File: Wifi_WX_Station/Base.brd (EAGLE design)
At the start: 100 x 81.3 mm, 62 parts, among them IC1 25LC512, IC2 3.3v, IC3 PIC24FJ128GA008, Q2 32Khz, X1 MINI-USB-VERT

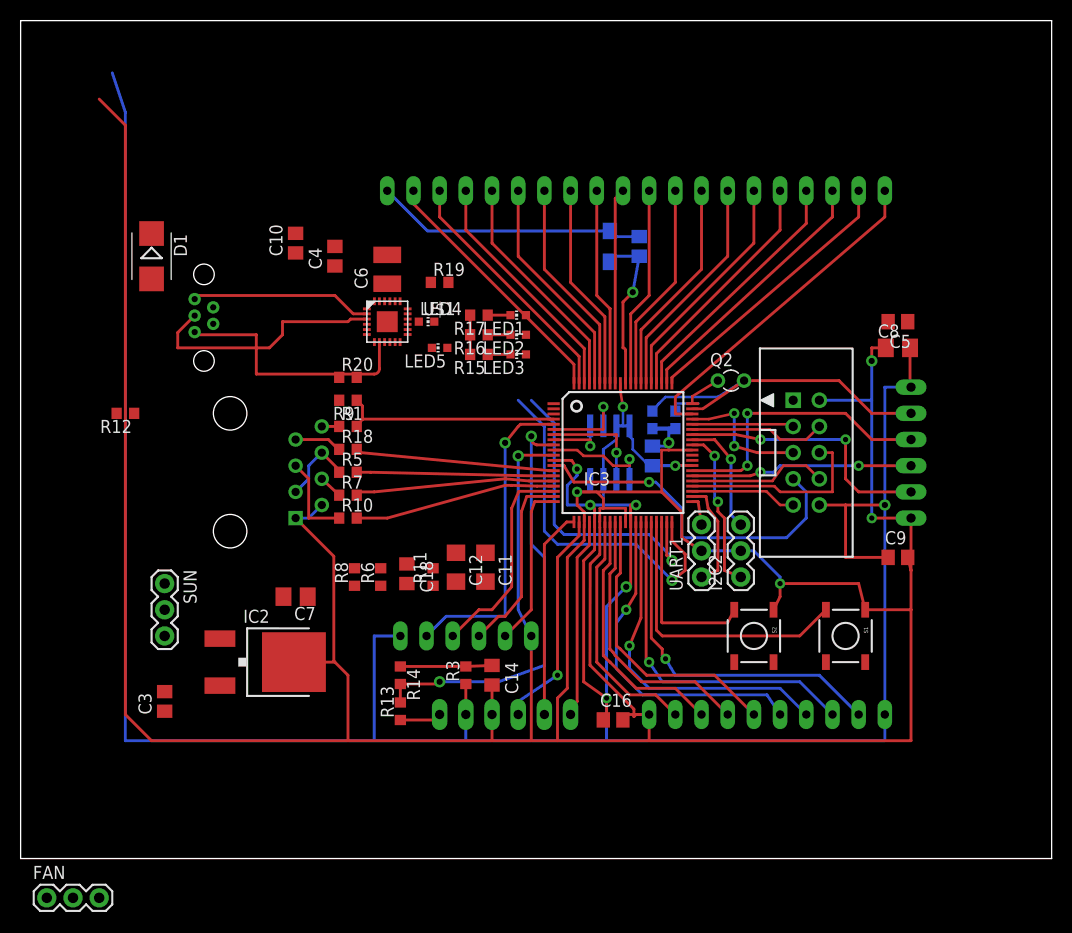
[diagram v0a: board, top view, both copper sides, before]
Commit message: added all the small boards, renamed Wifi module as RH and LH version
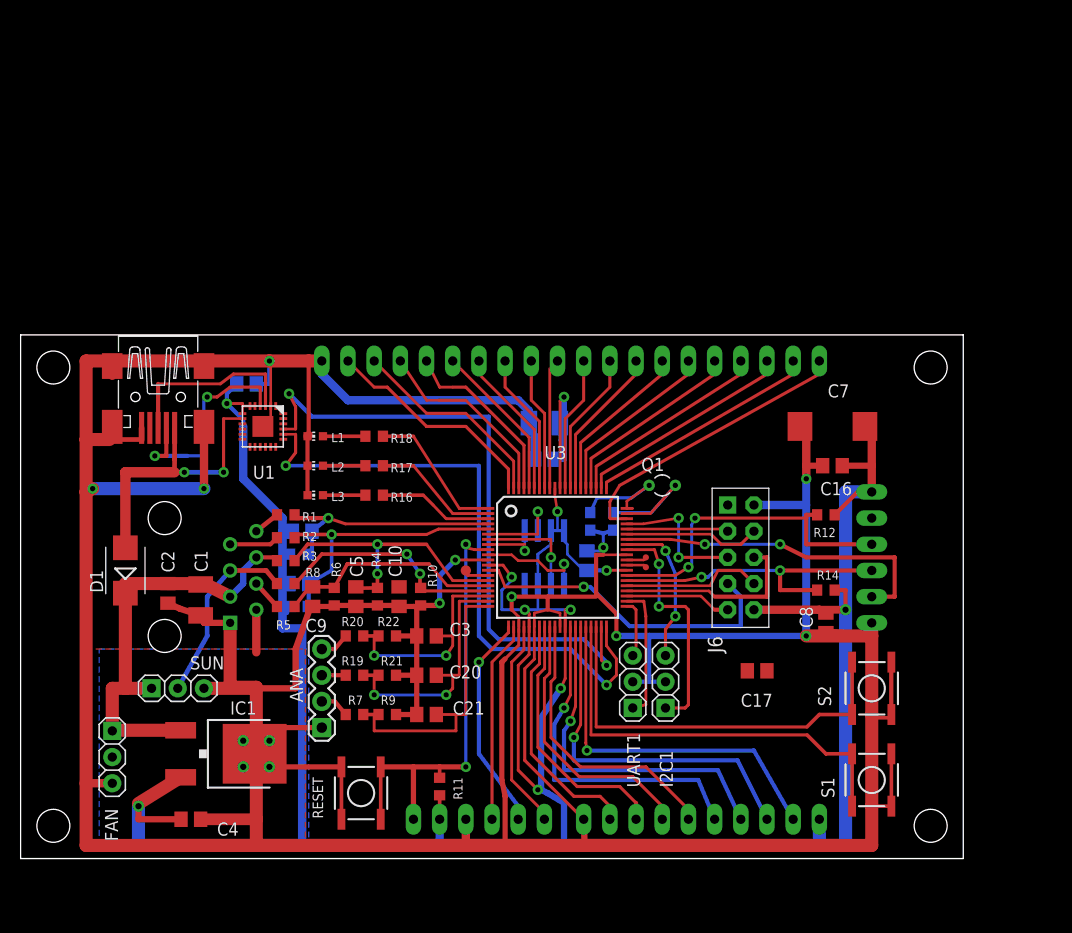
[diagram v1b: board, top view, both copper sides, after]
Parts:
- removed ANA_IN: (no value), con-lsta:FE06
- removed BHT: MA1X06, wifi_WX:1X06
- removed I2C2: (no value), SparkFun-Connectors:1X03
- removed IC2: 3.3v, Stofer:DPACK
- removed IC3: PIC24FJ128GA008, wifi_WX:TQFP80-12X12
- removed JP1: (no value), wifi_WX:1X06_PIKIT
- removed JP2: M05X2SHD, wifi_WX:2X5-SHROUDED
- removed LED1, LED2, LED3, LED4, LED5: (no value), led:CHIP-LED0603
- removed Q2: 32Khz, crystal:TC26V
- removed U$1: CP2104-GM, wifi_WX:QFN24_4X4
- removed U$3: RJ45-8VERT, wifi_WX:RJ45_VERT
- removed X1: MINI-USB-VERT, wifi_WX:USB_MINI_VERT
- added ANA: (no value), SparkFun-Connectors:1X04
- added C19, C20, C21: 0.1uF, rcl:C0805
- added I2C1: (no value), wifi_WX:1X03
- added J1: RJ45-8VERT, wifi_WX:RJ45_VERT
- added J5: MA1X06, wifi_WX:1X06
- added J6: M05X22X5FE, wifi_WX:2X5FEMALE
- added JPROG: (no value), wifi_WX:1X06_PIKIT
- added L1: grn, led:CHIP-LED0603
- added L2: ambr, led:CHIP-LED0603
- added L3: red, led:CHIP-LED0603
- added Q1: 32Khz, crystal:TC26V
- added R2: 120o, rcl:R0603
- added R21, R22: 26.1K, rcl:R0603
- added R4: 10k, rcl:R0603
- added RESET: SWITCH-MOMENTARY-2SMD, SparkFun-Electromechanical:TACTILE_SWITCH_SMD
- added TP1, TP2: TPTP06R, 1AA_Stofer:TP06R
- added TP3: TPTP10R, 1AA_Stofer:TP10R
- added U1: CP2104-GM, wifi_WX:QFN24_4X4
- added U2: 25LC512, microchip:SO-08
- added U3: PIC24FJ128GA008, wifi_WX:TQFP80-12X12
- added USB: MINI-USB-32005-301, wifi_WX:32005-301
- C1: value 22p -> 22u/10v; device rcl:C0603 -> rcl:SMC_B
- C10, C9: value 0.1u -> 2.2uF
- C11: value 2.2u -> 0.1uF; device rcl:C1206 -> rcl:C0805
- C12: value 2.2u -> 22uF/10V; device rcl:C1206 -> rcl:SMC_B
- C13: value 0.1uf -> 0.1uF
- C14: value 1u -> 22p; device rcl:C0805 -> rcl:C0603
- C15: value 10uf/6v -> 22p; device rcl:SMC_A -> rcl:C0603
- C16, C17, C18, C3, C4, C5: value 0.1u -> 0.1uF
- C2: value 22p -> 0.1uF; device rcl:C0603 -> rcl:C0805
- C6: value 4.7u -> 0.1uF; device rcl:C1210 -> rcl:C0805
- C7: value 22u/10v -> 330uF/6V; device rcl:R/2012-12R -> rcl:SMC_D
- C8: value 100u/4v -> 0.1uF; device rcl:R/2012-12R -> rcl:C0805
- FAN, SUN, UART1: device SparkFun-Connectors:1X03 -> wifi_WX:1X03
- IC1: value 25LC512 -> 3.3v; device microchip:SO-08 -> Stofer:DPACK
- R1: value 120 -> 120o
- R10: value 14k -> 26.1K
- R11: value 26.4K -> 10k
- R12: value 4.7k -> 4.7K
- R13: value 120 -> 4.7k
- R14: value 10k -> 4.7K
- R15: value 1k -> 4.7k
- R18: value 120 -> 470o
- R19, R20: value 1k -> 14k
- R5: value 10k -> 8.2k
- R6: value 10k -> 26.1k
- R7: value 6.8k -> 14k
- R8: value 26.4K -> 14k
- R9: value 4.7k -> 26.1K
- SV1, SV2, SV3: device con-lsta:FE10 -> wifi_WX:FE10
- moved R12 68.7 mm to (78.1, 33.3)
- moved C5 59.0 mm to (32.5, 25.4), turned to 270 degrees
- moved C9 56.9 mm to (28.3, 25.4), turned to 270 degrees
- moved C4 56.4 mm to (16.5, 3.81), turned to 0 degrees
- moved C7 54.6 mm to (78.7, 41.9)
- moved C2 52.0 mm to (14.3, 25.7), flipped to the top
- moved C1 47.2 mm to (17.5, 25.1), flipped to the top
- moved IC1 47.0 mm to (20.3, 10.2), flipped to the top, turned to 270 degrees
- moved R14 42.1 mm to (78.1, 26.0), turned to 180 degrees
- moved R19 39.0 mm to (32.4, 17.8)
- moved C10 35.7 mm to (36.7, 25.4), turned to 270 degrees
- moved C16 32.6 mm to (78.7, 38.1), turned to 180 degrees
- moved R9 30.7 mm to (35.6, 14.0)
- moved D1 30.6 mm to (10.2, 27.9), turned to 90 degrees
- moved R15 30.0 mm to (27.0, 24.4), flipped to the bottom, turned to 0 degrees
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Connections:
- removed net N$43: ANA_IN.5, IC3.20
- removed net N$46: LED4.A, R19.1
- removed net N$64: ANA_IN.4, IC3.19
- removed net N$65: ANA_IN.3, IC3.18
- removed net N$67: LED5.A, R20.1
- removed net N$68: LED4.C, U$1.14
- removed net N$69: LED5.C, U$1.13
- new net N$14: TP2.TP, U3.49
- new net N$18: L3.A, R16.2
- new net N$20: L2.A, R17.2
- new net N$21: L1.A, R18.2
- new net N$4: TP1.TP, U3.50
- new net N$5: R18.1, U3.1
- net +3V3: now also C11.2, C18.1, C19.2, C6.1, C7.+, C8.1, J5.6, J6.10, JPROG.2, R11.1, R12.1, R13.2, R14.1, R15.2, U1.5, U1.6, U1.7, U2.3, U2.7, U2.8, U3.12, U3.25, U3.32, U3.48, U3.71; no longer ANA_IN.1, BHT.6, C3.1, C5.1, C8.+, C9.1, IC1.7, IC1.8, IC2.3, IC3.12, IC3.25, IC3.32, IC3.48, IC3.71, JP1.2, JP2.10, R12.2, R19.2, R20.2, R3.1, R9.2, U$1.5, U$1.6, U$1.7
- net +5V: now also C1.+, C2.1, FAN.1, IC1.1, J1.P$3, J1.P$6, R3.1; no longer C10.1, C7.+, IC2.1, R5.1, U$3.P$3, U$3.P$6
- net BARO_CS: now also J5.2, U3.54; no longer BHT.2, IC3.54
- net GND: now also ANA.1, C1.-, C12.-, C15.2, C20.2, C21.2, C8.2, FAN.3, I2C1.2, J1.P$1, J1.P$2, J5.1, J6.2, JPROG.3, L1.C, L2.C, L3.C, R10.1, R21.1, R22.1, R4.1, R9.1, RESET.3, RESET.4, S1.2, S2.2, U1.2, U1.25, U2.4, U3.11, U3.23, U3.26, U3.31, U3.51, USB.5_USB_GND, USB.M1, USB.M2, USB.M3, USB.M4; no longer ANA_IN.6, BHT.1, C1.2, C11.2, C12.2, C15.-, C8.-, I2C2.2, IC2.4, IC3.11, IC3.23, IC3.26, IC3.31, IC3.51, JP1.3, JP2.2, R11.1, R15.2, R16.2, R17.2, R8.1, U$1.2, U$1.25, U$3.P$1, U$3.P$2, X1.P$5
- net MCU_RESET_: now also JPROG.1, R11.2, RESET.1, RESET.2, U3.9; no longer IC3.9, R13.2, R14.2
- net MRF_CS_: now also J6.5, U3.57; no longer IC3.57, JP2.5
- net MRF_HIBER: now also J6.3, U3.56; no longer IC3.56, JP2.3
- net MRF_RESET_: now also J6.4, U3.55; no longer IC3.55, JP2.4
- net MRF_SCK: now also J6.8, U3.45; no longer IC3.45, JP2.8
- net MRF_SDI: now also J6.9, U3.43; no longer IC3.43, JP2.9
- net MRF_SDO: now also J6.6, U3.44; no longer IC3.44, JP2.6
- net N$1: now also I2C1.1, U3.52; no longer I2C2.1, IC3.52
- net N$10: now also U3.61; no longer IC3.61
- net N$11: now also U3.62; no longer IC3.62
- net N$12: now also U3.63; no longer IC3.63
- net N$13: now also U3.64; no longer IC3.64
- net N$15: now also U3.65; no longer IC3.65
- net N$16: now also JPROG.5, U3.21; no longer IC3.21, JP1.5
- net N$17: now also JPROG.4, U3.22; no longer IC3.22, JP1.4
- net N$19: now also C12.+, U3.70; no longer C15.+, IC3.70
- net N$2: now also C15.1, Q1.2, U3.59; no longer BHT.5, C1.1, IC3.59, Q2.2
- net N$22: now also C21.1, R7.2, R9.2, U3.20; no longer C14.1, R14.1, R3.2
- net N$23: now also ANA.4, R20.1; no longer LED1.C, R17.1
- net N$24: now also C20.1, R19.2, R21.2, U3.19; no longer JP1.1, R13.1
- net N$25: now also U2.2, U3.7; no longer IC1.2, IC3.7
- net N$26: now also U3.66; no longer IC3.66
- net N$27: now also U2.1, U3.10; no longer IC1.1, IC3.10
- net N$28: now also C3.1, R20.2, R22.2, U3.18; no longer LED2.C, R16.1
- net N$29: now also U2.6, U3.6; no longer IC1.6, IC3.6
- net N$3: now also C10.1; no longer C6.1, U$1.16
- net N$30: now also ANA.3, R19.1; no longer LED3.C, R15.1
- net N$31: now also ANA.2, R7.1; no longer IC3.1, LED1.A
- net N$32: now also U2.5, U3.8; no longer IC1.5, IC3.8
- net N$33: now also R17.1, U3.2; no longer IC3.2, LED2.A
- net N$34: now also R16.1, U3.3; no longer IC3.3, LED3.A
- net N$35: now also U3.67; no longer IC3.67
- net N$36: now also U3.68; no longer IC3.68
- net N$37: now also S2.4, U3.38; no longer IC3.38
- net N$38: now also S1.4, U3.37; no longer IC3.37
- net N$40: now also U3.69; no longer IC3.69
- net N$41: now also U3.72; no longer IC3.72
- net N$42: now also U3.58; no longer IC3.58
- net N$44: now also U3.41; no longer IC3.41
- net N$45: now also U3.42; no longer IC3.42
- net N$47: now also U3.27; no longer IC3.27
- net N$48: now also U3.28; no longer IC3.28
- net N$49: now also U3.29; no longer IC3.29
- net N$50: now also U3.30; no longer IC3.30
- net N$51: now also U3.33; no longer IC3.33
- net N$52: now also U3.34; no longer IC3.34
- net N$53: now also U3.35; no longer IC3.35
- net N$54: now also U3.36; no longer IC3.36
- net N$55: now also U3.73; no longer IC3.73
- net N$56: now also U3.74; no longer IC3.74
- net N$57: now also U3.75; no longer IC3.75
- net N$58: now also U3.76; no longer IC3.76
- net N$59: now also U3.77; no longer IC3.77
- net N$6: now also I2C1.3, U3.53; no longer I2C2.3, IC3.53
- net N$60: now also U3.78; no longer IC3.78
- net N$61: now also U3.79; no longer IC3.79
- net N$62: now also U3.80; no longer IC3.80
- net N$63: now also JPROG.6, U3.24; no longer IC3.24, JP1.6
- net N$66: now also C5.1, R3.2, R4.2, U3.15; no longer C18.1, IC3.15, R5.2, R6.2
- net N$7: now also C14.1, Q1.1, U3.60; no longer C2.1, IC3.60, Q2.1
- net N$8: now also TP3.TP, U3.14; no longer ANA_IN.2, IC3.5
- net N$9: now also U1.8, USB.1_VBUS; no longer U$1.8, X1.P$1
- net RAIN_CNT_IN: now also J1.P$7, R2.1; no longer R18.1, U$3.P$7
- net RAIN_COUNT: now also C11.1, R15.1, R2.2, U3.5; no longer IC3.14, R12.1, R18.2
- net SCL1: now also J5.4, R12.2, U3.47; no longer BHT.4, IC3.47
- net SDA1: now also J5.3, R14.2, U3.46; no longer BHT.3, IC3.46
- net SUN_ADC_IN: now also R8.2, U3.17; no longer C12.1, IC3.17, R11.2
- net SUN_IN: now also J1.P$5, R8.1; no longer R10.1, U$3.P$5
- net USB_D+: now also U1.3, USB.3_D+; no longer U$1.3, X1.P$3
- net USB_D-: now also U1.4, USB.2_D-; no longer U$1.4, X1.P$2
- net USB_RXD: now also U1.20, U3.40; no longer IC3.40, U$1.20
- net USB_TXD: now also U1.21, U3.39; no longer IC3.39, U$1.21
- net WIFI_INT_: now also J6.7, U3.13; no longer IC3.13, JP2.7
- net WIND_ADC_IN: now also C9.1, R5.2, R6.2, U3.16; no longer C11.1, IC3.16, R7.2, R8.2
- net WIND_COUNT: now also C19.1, R13.1, U3.4; no longer IC3.4, R9.1
- net WIND_COUNT_IN: now also J1.P$8; no longer U$3.P$8
- net WIN_DIR_IN: now also J1.P$4, R5.1; no longer R7.1, U$3.P$4
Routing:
- net GND: track 424.0 -> 553.0 mm, vias 6 -> 14
- net +5V: track 7.47 -> 42.3 mm
- net USB_TXD: track 30.0 -> 62.7 mm, vias 1 -> 2
- net N$8: track 30.8 -> 2.51 mm, vias 1 -> 0
- net USB_RXD: track 34.9 -> 60.5 mm, vias 1 -> 2
- net N$37: track 17.6 -> 40.1 mm
- net USB_D-: track 0.00 -> 21.9 mm, vias 0 -> 2
- net N$24: track 4.03 -> 25.2 mm, vias 0 -> 2
- net N$65: track 20.6 -> 0.00 mm
- net N$2: track 33.3 -> 13.2 mm
- net N$22: track 8.89 -> 28.5 mm
- net N$28: track 2.21 -> 21.4 mm, vias 0 -> 2
- net N$64: track 18.2 -> 0.00 mm
- net N$43: track 16.0 -> 0.00 mm
- net N$5: track 0.00 -> 14.0 mm
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- added copper zone on layer 1, net GND
- added copper zone on layer 16, net GND
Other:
- board size 100 x 81.3 mm -> 91.4 x 50.8 mm
- board text added: "1"
- board text added: "RV-BUILDERS PRODUCTS 2013"
- board text added: "Wunder Weather Station"

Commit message: updated BOM with all prices- As Checked in to BATCH PCB
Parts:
- removed C17: 0.1uF, rcl:C0805
- added R23, R24: 4.7K, rcl:R0603
- ANA: device SparkFun-Connectors:1X04 -> wifi_WX:1X04
- FAN, SUN: device wifi_WX:1X03 -> wifi_WX:1X3_MOLEX_KK
- IC1: device Stofer:DPACK -> wifi_WX:DPACK
- J5: value MA1X06 -> (none); device wifi_WX:1X06 -> wifi_WX:1X5_MOLEX_KK
- Q1: value 32Khz -> 32.768Khz; device crystal:TC26V -> wifi_WX:CRYSTAL32_SMT
- RESET, S1, S2: device SparkFun-Electromechanical:TACTILE_SWITCH_SMD -> wifi_WX:TACTILE_SWITCH_SMD
- SV1, SV2, SV3: value (none) -> M10"; device wifi_WX:FE10 -> wifi_WX:1X10
- TP1, TP2: value TPTP06R -> TP; device 1AA_Stofer:TP06R -> wifi_WX:TP06R
- TP3: value TPTP10R -> TP; device 1AA_Stofer:TP10R -> wifi_WX:TP06R
- moved TP1 17.5 mm to (43.2, 27.9)
- moved TP3 17.1 mm to (60.3, 28.3)
- moved SV1 11.4 mm to (54.6, 3.81)
- moved SV3 11.4 mm to (52.1, 48.3)
- moved SV2 11.4 mm to (77.5, 48.3)
- moved I2C1 10.8 mm to (72.4, 12.7), turned to 0 degrees
- moved J5 7.10 mm to (79.4, 22.9)
- moved Q1 5.85 mm to (63.5, 41.9), flipped to the bottom
- moved UART1 5.28 mm to (62.2, 12.7), turned to 180 degrees
- moved FAN 4.96 mm to (12.1, 13.7), flipped to the bottom
- moved SUN 4.07 mm to (12.7, 13.3)
- moved R12 2.22 mm to (75.9, 33.3), turned to 270 degrees
- moved R14 2.22 mm to (75.9, 26.0), turned to 90 degrees
- moved RESET 1.91 mm to (31.1, 6.35)
- moved IC1 1.42 mm to (19.1, 9.53)
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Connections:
- removed net N$1: I2C1.1, U3.52
- removed net N$3: C10.1
- removed net N$6: I2C1.3, U3.53
- new net SCL2: I2C1.1, R24.2, U3.52
- new net SDA2: I2C1.3, R23.2, U3.53
- net +3V3: now also J5.5, R23.1, R24.1; no longer C17.1, J5.6
- net GND: no longer C17.2
- net N$14: now also TP3.TP_1; no longer TP2.TP
- net N$2: now also Q1.P$3; no longer Q1.2
- net N$4: now also TP2.TP_1; no longer TP1.TP
- net N$7: now also Q1.P$2; no longer Q1.1
- net N$8: now also TP1.TP_1; no longer TP3.TP
- net SUN_ADC_IN: now also C10.1
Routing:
- net GND: track 553.0 -> 590.7 mm
- net SCL2: track 0.00 -> 30.5 mm, vias 0 -> 3
- net SDA2: track 0.00 -> 29.7 mm, vias 0 -> 2
- net N$1: track 22.8 -> 0.00 mm, vias 2 -> 0
- net N$6: track 14.8 -> 0.00 mm, vias 2 -> 0
- net N$44: track 5.79 -> 14.6 mm
- net N$7: track 10.9 -> 16.8 mm, vias 0 -> 1
- net SDA1: track 29.6 -> 25.0 mm
- net N$45: track 13.0 -> 16.8 mm
- net N$37: track 40.1 -> 43.6 mm
- net SCL1: track 32.4 -> 29.0 mm
- net +3V3: track 299.0 -> 296.5 mm
- net +5V: track 42.3 -> 44.5 mm, vias 0 -> 1
- net SUN_ADC_IN: track 22.7 -> 24.7 mm
- net MCU_RESET_: track 43.6 -> 45.5 mm
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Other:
- board text added: "Baro & Hygro"
- board text added: "J6"
- board text added: "This is NOT an Ethernet port"
- board text added: "WiFi"

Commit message: Wind speed board and base station rework to rev HW 1.2
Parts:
- added +5V: (no value), wifi_WX:1X3_MOLEX_KK
- added D2: MBR0520LT, diode:SOD123
- added RAIN: M02, wifi_WX:1X02
- ANA: device wifi_WX:1X04 -> wifi_WX:1X05
- R13: value 4.7k -> 2.2K
- TP1: value TP -> TP10R; device wifi_WX:TP06R -> wifi_WX:TP10R
- TP2, TP3: value TP -> TP6R
- moved UART1 15.7 mm to (77.5, 8.89), turned to 90 degrees
- moved I2C1 6.35 mm to (77.5, 16.5), turned to 90 degrees
- moved FAN 4.14 mm to (12.4, 17.8)
- moved C3 2.62 mm to (40.0, 19.1)
- moved R22 2.62 mm to (36.2, 19.1)
- moved R20 2.54 mm to (32.4, 19.1)
- moved C20 1.42 mm to (40.0, 16.5)
- moved R21 1.42 mm to (36.2, 16.5)
- moved JPROG 1.27 mm to (43.2, 3.81)
- moved R11 1.27 mm to (39.4, 6.99)
- moved S1 1.27 mm to (82.5, 6.35)
- moved ANA 1.27 mm to (29.2, 11.4)
- moved R19 1.27 mm to (32.4, 16.5)
- moved C21 0.64 mm to (40.0, 14.0)
- moved R9 0.63 mm to (36.2, 14.0)
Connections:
- new net N$1: D2.C, R2.2
- net +5V: now also +5V.1, ANA.5
- net GND: now also +5V.3, RAIN.1
- net RAIN_CNT_IN: now also RAIN.2
- net RAIN_COUNT: now also D2.A; no longer R2.2
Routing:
- net GND: track 590.7 -> 612.1 mm, vias 14 -> 15
- net N$45: track 16.8 -> 34.4 mm, vias 0 -> 1
- net N$44: track 14.6 -> 31.8 mm
- net +5V: track 44.5 -> 55.6 mm, vias 1 -> 0
- net USB_D-: track 21.9 -> 13.7 mm, vias 2 -> 0
- net RAIN_CNT_IN: track 4.81 -> 12.6 mm
- net N$1: track 0.00 -> 6.35 mm
- net N$9: track 28.2 -> 23.5 mm, vias 2 -> 0
- net SCL2: track 30.5 -> 34.9 mm, vias 3 -> 4
- net RAIN_COUNT: track 27.5 -> 23.9 mm
- net N$28: track 21.4 -> 24.3 mm
- net +3V3: track 296.5 -> 294.6 mm
- net USB_RXD: track 60.5 -> 59.3 mm
- net WIND_COUNT: track 24.2 -> 25.1 mm
- net SUN_ADC_IN: track 24.7 -> 25.6 mm
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
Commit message: Revision B.1
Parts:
- C5: value 0.1uF -> 2.2uF
- moved Q1 1.27 mm to (63.5, 40.6)
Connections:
- removed net N$37: S2.3, S2.4, U3.38
- removed net N$38: S1.3, S1.4, U3.37
- new net SW_S1: S1.3, S1.4, U1.13, U3.37
- new net SW_S2: S2.3, S2.4, U1.12, U3.38
- net MCU_RESET_: now also U1.14
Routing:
- net SW_S2: track 0.00 -> 100.4 mm, vias 0 -> 4
- net SW_S1: track 0.00 -> 96.1 mm, vias 0 -> 4
- net N$37: track 43.3 -> 0.00 mm
- net N$38: track 42.6 -> 0.00 mm
- net MCU_RESET_: track 45.5 -> 75.1 mm, vias 2 -> 3
- net GND: track 612.1 -> 619.7 mm
- net WIFI_INT_: track 31.8 -> 33.8 mm
- net N$2: track 13.0 -> 11.8 mm
- net N$7: track 16.8 -> 15.5 mm
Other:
- board text added: "NOT Ethernet !"
- board text added: "PCB Revision B.2"
- board text added: "PIC24FJ256GA108"
- board text removed: "This is NOT an Ethernet port"

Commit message: 
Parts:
- C9: value 2.2uF -> 0.1uF
- R6: value 26.1k -> 26.1K
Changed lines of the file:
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@@
 <attribute name="NAME" x="24.765" y="22.225" size="0.889" layer="25"/>
 </element>
-<element name="R6" library="rcl" package="R0603" value="26.1k" x="30.4165" y="25.4" smashed="yes" rot="R90">
+<element name="R6" library="rcl" package="R0603" value="26.1K" x="30.4165" y="25.4" smashed="yes" rot="R90">
 <attribute name="NAME" x="31.0515" y="27.305" size="0.889" layer="25" rot="R90"/>
 </element>
-<element name="C9" library="rcl" package="C0805" value="2.2uF" x="28.321" y="25.4" smashed="yes" rot="R270">
+<element name="C9" library="rcl" package="C0805" value="0.1uF" x="28.321" y="25.4" smashed="yes" rot="R270">
 <attribute name="NAME" x="27.559" y="21.2725" size="1.016" layer="25" rot="R90"/>
 </element>

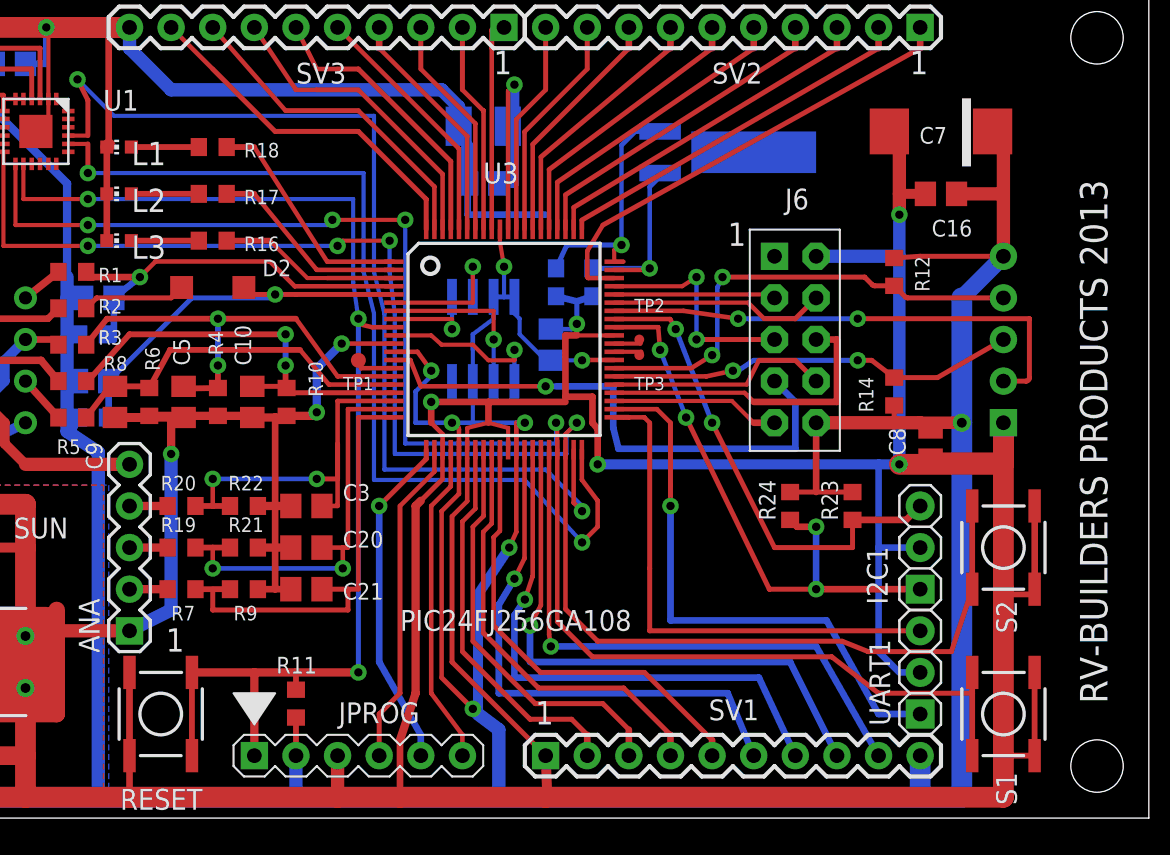
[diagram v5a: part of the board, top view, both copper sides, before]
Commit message: Changed to RJ11 connector for Baro_temp_hyg  on base board -- Cleaned up some silk screen stuff Added new RJ11 based Baro_Temp_Hyg board layout
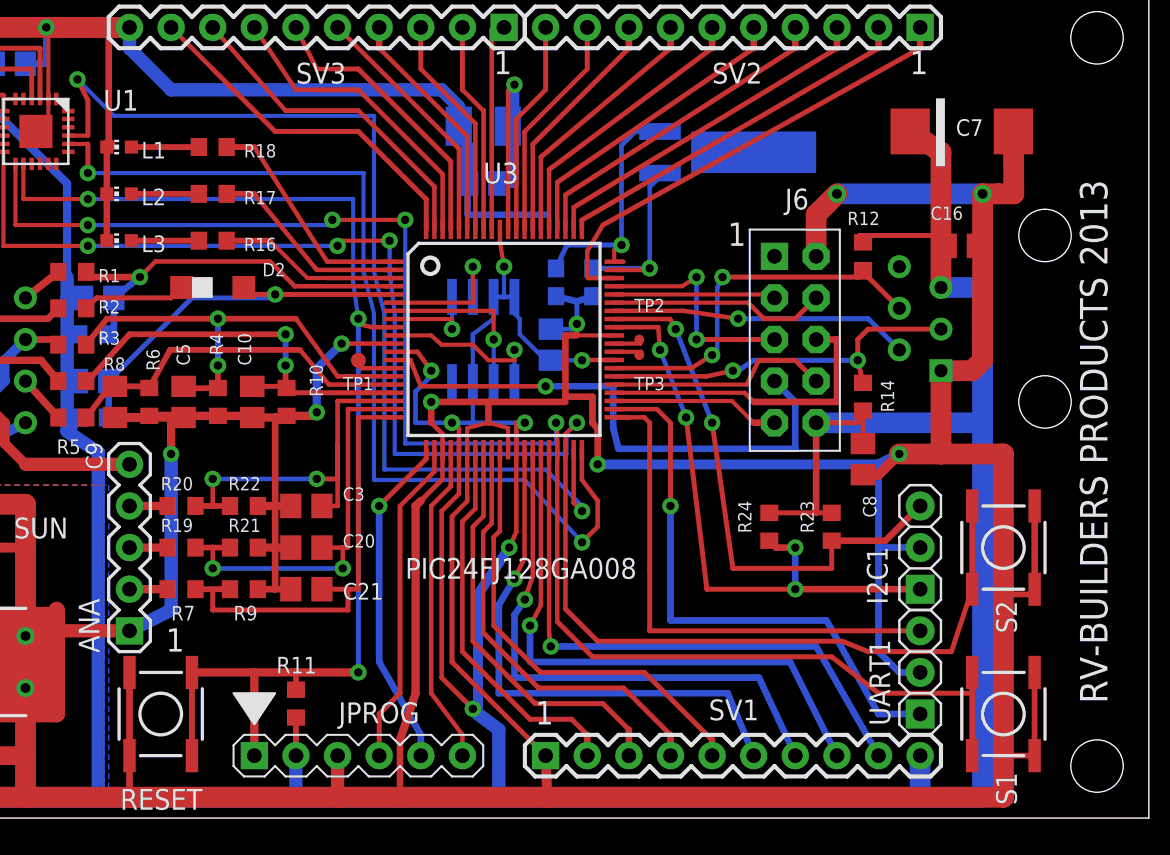
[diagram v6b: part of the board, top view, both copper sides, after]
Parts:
- J5: value (none) -> RJ11-6RJ11-VERT_LP; device wifi_WX:1X5_MOLEX_KK -> wifi_WX:RJ11-6-VERT
- moved J5 8.26 mm to (82.5, 30.5), turned to 270 degrees
- moved C8 4.24 mm to (74.0, 21.9)
- moved C16 3.42 mm to (80.0, 34.9), turned to 0 degrees
- moved R12 2.13 mm to (74.0, 34.3)
- moved R14 1.93 mm to (74.0, 25.7)
- moved R23 1.80 mm to (72.1, 17.8)
- moved R24 1.80 mm to (68.3, 17.8)
- moved C7 1.27 mm to (80.0, 41.9), turned to 0 degrees
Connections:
- net +3V3: now also J5.P$5; no longer J5.5
- net BARO_CS: now also J5.P$2; no longer J5.2
- net GND: now also J5.P$1; no longer J5.1
- net SCL1: now also J5.P$4; no longer J5.4
- net SDA1: now also J5.P$3; no longer J5.3
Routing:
- net BARO_CS: track 30.7 -> 18.2 mm, vias 2 -> 1
- net +3V3: track 294.6 -> 301.0 mm, vias 10 -> 9
- net SCL1: track 29.0 -> 23.5 mm
- net SDA2: track 29.7 -> 33.2 mm
- net GND: track 619.7 -> 621.8 mm, vias 15 -> 16
- net SDA1: track 25.0 -> 23.1 mm
- net SCL2: track 34.9 -> 36.4 mm
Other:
- board text added: "Baro-Temp-Hyg"
- board text removed: "Baro & Hygro"
- board text removed: "PIC24FJ256GA108"
